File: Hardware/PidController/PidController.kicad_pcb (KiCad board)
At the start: 2 copper layers, 100.3 x 60.3 mm, 43 parts, among them J1 Conn_01x03, J2 Conn_01x03, J3 Conn_01x04, J4 Conn_01x06, J5 Motor_x02, J6 Conn_01x04, Q1 BC817, Q2 BTA16-600B, T1 GG_Transformer_1P_1S, U1 LM317_TO-220, U2 Arduino_Pro_mini, U3 MOC3023M

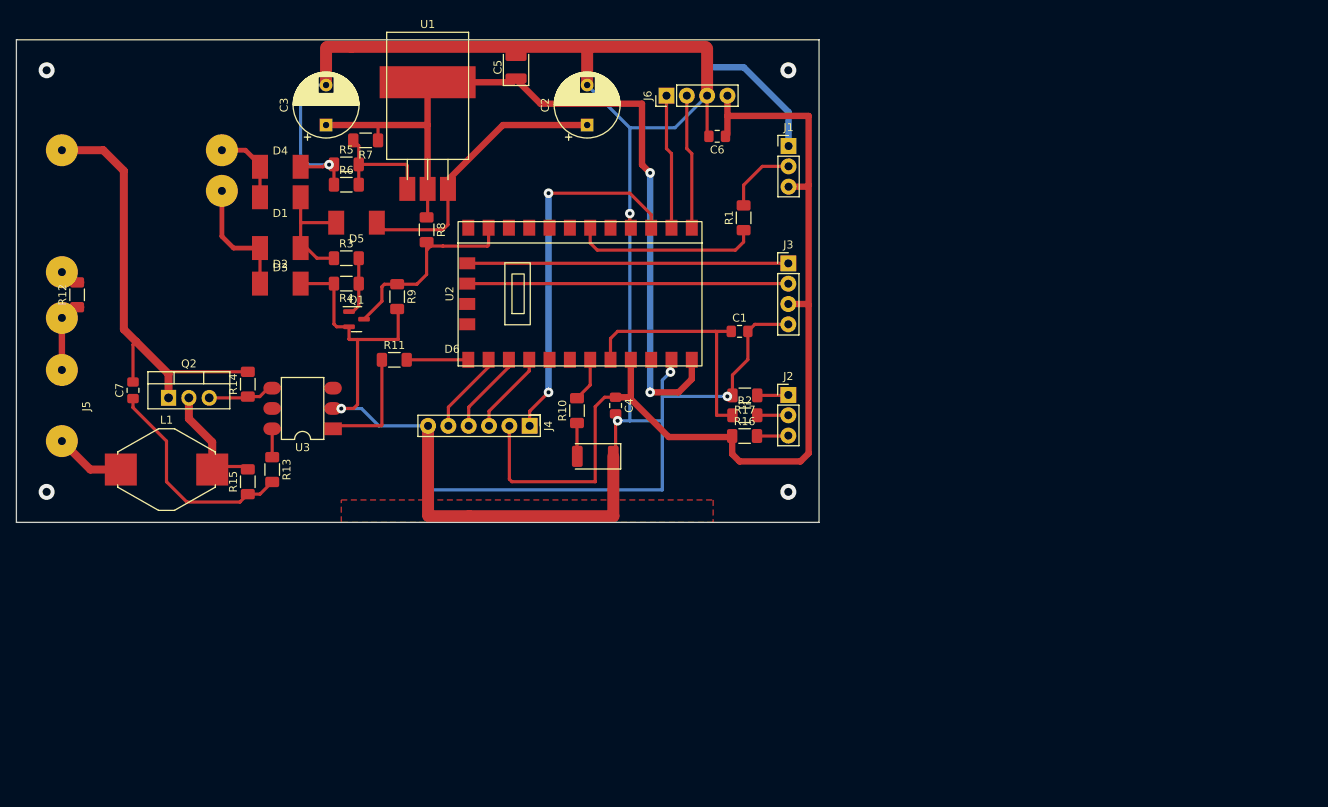
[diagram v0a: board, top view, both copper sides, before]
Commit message: First tests done, first PID params tuning
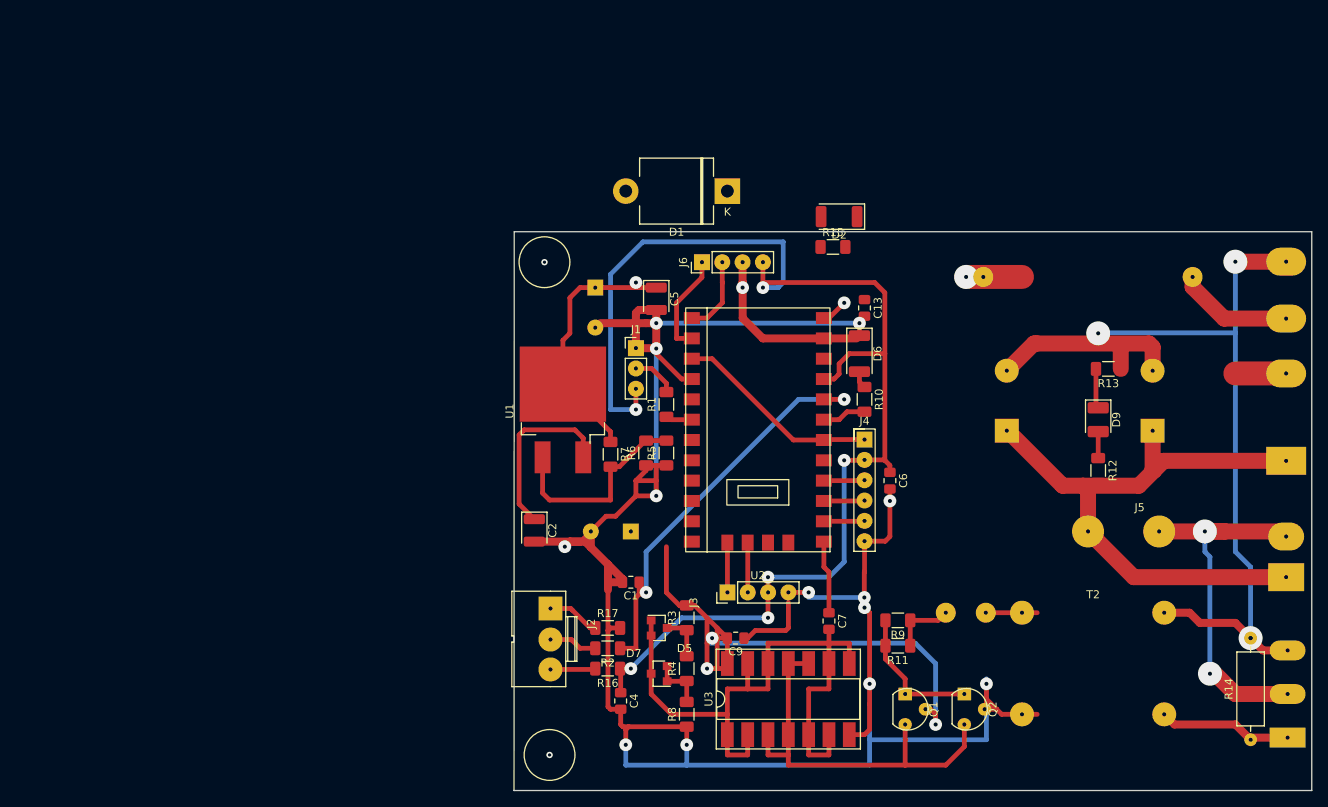
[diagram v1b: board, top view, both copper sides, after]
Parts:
- removed D3, D4: D, PCB_Library:D_SMD_L
- removed L1: L, PCB_Library:L_2R2_SMD
- removed T1: GG_Transformer_1P_1S, PCB_Library:Transformer_2VA_1xSec
- added C10: 100mf, PCB_Library:CP_Radial_D18.0mm_P7.50mm, B.Cu at (149.2, 70.6)
- added C11: 4.7uF, PCB_Library:C_Film_5.08, B.Cu at (141.6, 93.3)
- added C12: 1000mF, PCB_Library:CP_Radial_D8.0mm_P5.00mm, B.Cu at (102.2, 83.2)
- added C13: 100nF, Capacitor_SMD:C_0805_2012Metric_Pad1.18x1.45mm_HandSolder, F.Cu at (131.4, 55.2)
- added C8: 100mf, PCB_Library:CP_Radial_D18.0mm_P7.50mm, B.Cu at (167.5, 70.6)
- added C9: 100nF, Capacitor_SMD:C_0805_2012Metric_Pad1.18x1.45mm_HandSolder, F.Cu at (115.3, 96.5)
- added D10: RHRP15120, PCB_Library:D_TO-220-2_Vertical, B.Cu at (184.2, 88.9)
- added D7: Bat54, PCB_Library:D_SOT-23_ANK, F.Cu at (105.8, 101.0)
- added D8: D_Bridge_-AA+, PCB_Library:Diode_Bridge_300V, B.Cu at (184.2, 67.2)
- added D9: LED, LED_SMD:LED_1210_3225Metric_Pad1.42x2.65mm_HandSolder, F.Cu at (160.7, 69.2)
- added F1: Fuse, PCB_Library:Fuse_5X20, B.Cu at (146.3, 51.4)
- added Q3: Q_NMOS_GDS, Package_TO_SOT_THT:TO-247-3_Vertical, B.Cu at (184.3, 109.0)
- added T2: Transformer_1P_1S, PCB_Library:Transformer_Toroid_Horizontal_D18.0mm, F.Cu at (152.4, 104.8)
- C2: value 220mF -> 100nF; footprint Capacitor_THT:CP_Radial_D8.0mm_P5.00mm -> LED_SMD:LED_1210_3225Metric
- C3: footprint Capacitor_THT:CP_Radial_D8.0mm_P5.00mm -> PCB_Library:CP_Radial_D8.0mm_P5.00mm; moved to B.Cu
- C7: value 0 -> 47nF
- D1: footprint PCB_Library:D_SMD_L -> Diode_THT:D_5KPW_P12.70mm_Horizontal
- D2: value D -> LED; footprint PCB_Library:D_SMD_L -> LED_SMD:LED_2010_5025Metric
- D5: value D -> Bat54; footprint PCB_Library:D_SMD_L -> PCB_Library:D_SOT-23_ANK
- J2: footprint PCB_Library:GG_PinHeader_1x03 -> PCB_Library:JWT_1x03_P3.96mm_Vertical
- Q1: value BC817 -> BC640; footprint Package_TO_SOT_SMD:SOT-23 -> PCB_Library:TO-92_delta
- Q2: value BTA16-600B -> BC639; footprint Package_TO_SOT_THT:TO-220-3_Vertical -> PCB_Library:TO-92_delta
- R1: value 220 -> 1K
- R11: value 220 -> 10
- R12: value 10 -> 47K
- R13: value 100 -> 47K
- R14: value 220 -> 100; footprint Resistor_SMD:R_1206_3216Metric_Pad1.30x1.75mm_HandSolder -> Resistor_THT:R_Axial_DIN0309_L9.0mm_D3.2mm_P12.70mm_Horizontal
- R15: value 100 -> 220
- R3: value 47k -> 1K
- R4, R8: value 4.7k -> 1K
- R5: value 47k -> 2.2K
- R6: value 47k -> NC
- R7: value 47k -> 220
- R9: value 4.7k -> 10
- U1: footprint PCB_Library:TO-220-3_Horizontal_SMD -> PCB_Library:TO-263-2
- U3: value MOC3023M -> 4071; footprint PCB_Library:MOC3023_W7.62mm -> Package_DIP:DIP-14_W8.89mm_SMDSocket_LongPads
- moved R14 133.0 mm to (179.7, 109.2)
- moved J5 132.0 mm to (161.9, 83.2), turned to 0 degrees
- moved R12 129.5 mm to (160.7, 75.6), turned to -90 degrees
- moved Q2 106.4 mm to (143.9, 104.1), turned to -90 degrees
- moved R13 105.3 mm to (161.9, 62.9), turned to 180 degrees
- moved C7 91.7 mm to (127.0, 94.4), turned to -90 degrees
- moved Q1 83.4 mm to (136.5, 104.1), turned to -90 degrees
- moved R15 78.8 mm to (127.5, 47.6), turned to 0 degrees
- moved R9 74.5 mm to (135.6, 94.3), turned to 180 degrees
- moved R11 72.4 mm to (135.6, 97.5), turned to 180 degrees
- moved D2 70.0 mm to (128.3, 43.8)
- moved R8 68.7 mm to (109.2, 106.0), turned to 90 degrees
- moved U3 66.2 mm to (121.9, 104.1), turned to 90 degrees
- moved R4 64.2 mm to (109.2, 100.3), turned to 90 degrees
- moved D5 63.2 mm to (105.8, 95.2), turned to 0 degrees
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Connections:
- C2 pad 1: Net-(C2-Pad1) -> +22V
- C3 pad 1: +7.5V -> /+14V
- C5 pad 1: +7.5V -> /+14V
- C7 pad 1: Net-(C7-Pad1) -> PWM
- C7 pad 2: AC220V_N -> Net-(C7-Pad2)
- D1 pad 1: Net-(D5-Pad2) -> Net-(D1-Pad1)
- D1 pad 2: AC10V_2 -> /+14V
- D2 pad 1: Net-(D5-Pad2) -> /+11V
- D2 pad 2: AC10V_1 -> Net-(D1-Pad1)
- D5 pad 1: Net-(C2-Pad1) -> Net-(D5-Pad1)
- D5 pad 2: Net-(D5-Pad2) -> Net-(C7-Pad2)
- J5 pad 1: AC220V_L -> Net-(C10-Pad1)
- Q1 pad 2: GND -> /+14V
- Q1 pad 3: ZERO_CROSS -> Net-(Q1-Pad3)
- Q2 pad 1: AC220V_N -> Net-(Q1-Pad1)
- Q2 pad 2: Net-(L1-Pad1) -> GND
- Q2 pad 3: Net-(Q2-Pad3) -> Net-(Q1-Pad3)
- R11 pad 1: Net-(R11-Pad1) -> Net-(C11-Pad1)
- R11 pad 2: Net-(R11-Pad2) -> Net-(Q1-Pad1)
- R12 pad 1: AC220V_L -> Net-(D9-Pad2)
- R12 pad 2: Net-(R12-Pad2) -> Net-(C10-Pad1)
- R13 pad 1: Net-(R13-Pad1) -> GNDPWR
- R13 pad 2: Net-(C7-Pad1) -> Net-(D9-Pad1)
- R14 pad 1: Net-(Q2-Pad3) -> Net-(Q3-Pad1)
- R14 pad 2: AC220V_N -> GNDPWR
- R15 pad 1: Net-(C7-Pad1) -> Net-(D1-Pad1)
- R15 pad 2: Net-(L1-Pad1) -> /+11V
- R3 pad 1: Net-(D5-Pad2) -> Net-(D5-Pad1)
- R3 pad 2: Net-(Q1-Pad1) -> /+14V
- R4 pad 1: Net-(Q1-Pad1) -> Net-(D7-Pad2)
- R4 pad 2: GND -> Net-(D5-Pad1)
- R7 pad 1: +7.5V -> /+14V
- R8 pad 1: +7.5V -> GND
- R8 pad 2: ZERO_CROSS -> Net-(D7-Pad2)
- R9 pad 1: ZERO_CROSS -> Net-(C11-Pad1)
- R9 pad 2: GND -> Net-(Q1-Pad1)
- U1 pad 2: +7.5V -> /+14V
- U1 pad 3: Net-(C2-Pad1) -> +22V
- U2 pad 1: Net-(R11-Pad2) -> PWM
- U2 pad 12: +7.5V -> /+11V
- U2 pad 23: ZERO_CROSS -> unconnected-(U2-Pad23)
- U2 pad 6: unconnected-(U2-Pad6) -> RST
- U3 pad 1: Net-(R11-Pad1) -> Net-(C7-Pad2)
- U3 pad 2: GND -> Net-(C7-Pad2)
- U3 pad 3: unconnected-(U3-Pad3) -> Net-(Q1-Pad3)
- U3 pad 4: Net-(Q2-Pad3) -> Net-(Q1-Pad3)
- U3 pad 5: unconnected-(U3-Pad5) -> Net-(C7-Pad2)
- U3 pad 6: Net-(R13-Pad1) -> Net-(C7-Pad2)
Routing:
- net +7.5V: track 133.3 -> 0.00 mm, vias 2 -> 0
- net GNDPWR: track 0.00 -> 117.4 mm, vias 0 -> 3
- net /+14V: track 0.00 -> 108.8 mm, vias 0 -> 4
- net Net-(C7-Pad2): track 0.00 -> 83.1 mm
- net Net-(C10-Pad1): track 0.00 -> 77.2 mm
- net Net-(Q1-Pad3): track 0.00 -> 51.1 mm
- net AC220V_N: track 54.7 -> 6.35 mm
- net Net-(D10-Pad2): track 8.84 -> 47.5 mm, vias 0 -> 2
- net GND: track 345.6 -> 309.5 mm, vias 6 -> 14
- net +5V: track 126.7 -> 162.5 mm, vias 0 -> 6
- net Net-(C2-Pad1): track 35.4 -> 0.00 mm
- net SCL: track 40.1 -> 6.24 mm
- net SDA: track 40.1 -> 6.24 mm
- net Net-(C7-Pad1): track 27.4 -> 0.00 mm
- net ZERO_CROSS: track 25.4 -> 0.00 mm
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- removed copper zone on F.Cu, net GND
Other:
- board size 100.3 x 60.3 mm -> 99.7 x 69.8 mm
